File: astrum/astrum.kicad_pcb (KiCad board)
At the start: 2 copper layers, 32 parts, among them J1 USB_C_Receptacle_USB2.0_16P, J2 Micro_SD_Card, U1 STM32H523CEUx, U10 BSS138DW-7-F, U2 LDL212PV33R, U3 USBLC6-2SC6, U4 W25Q32JVSS, U5 ICM-20948, U6 MIC5317-1.8xM5, U7 BSS138DW-7-F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

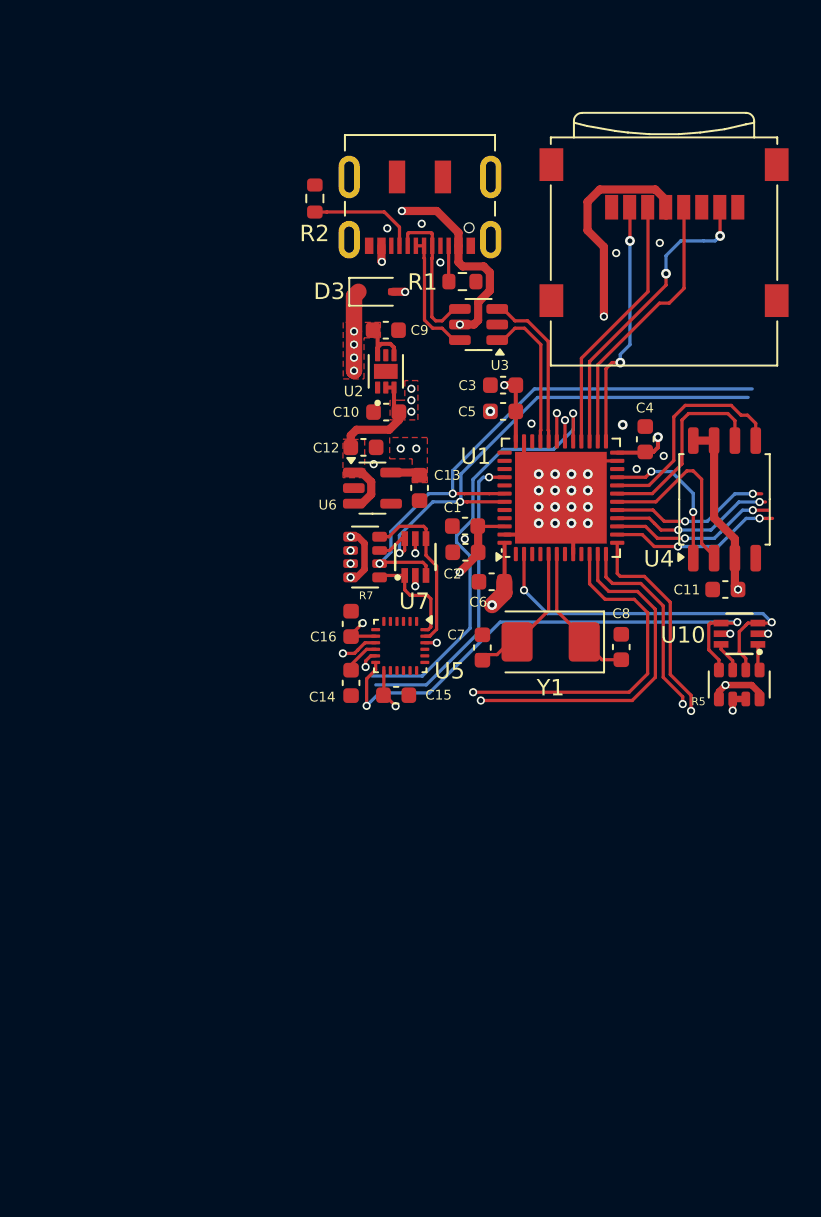
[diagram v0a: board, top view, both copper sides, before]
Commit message: add the drv routing and header pins + power supply
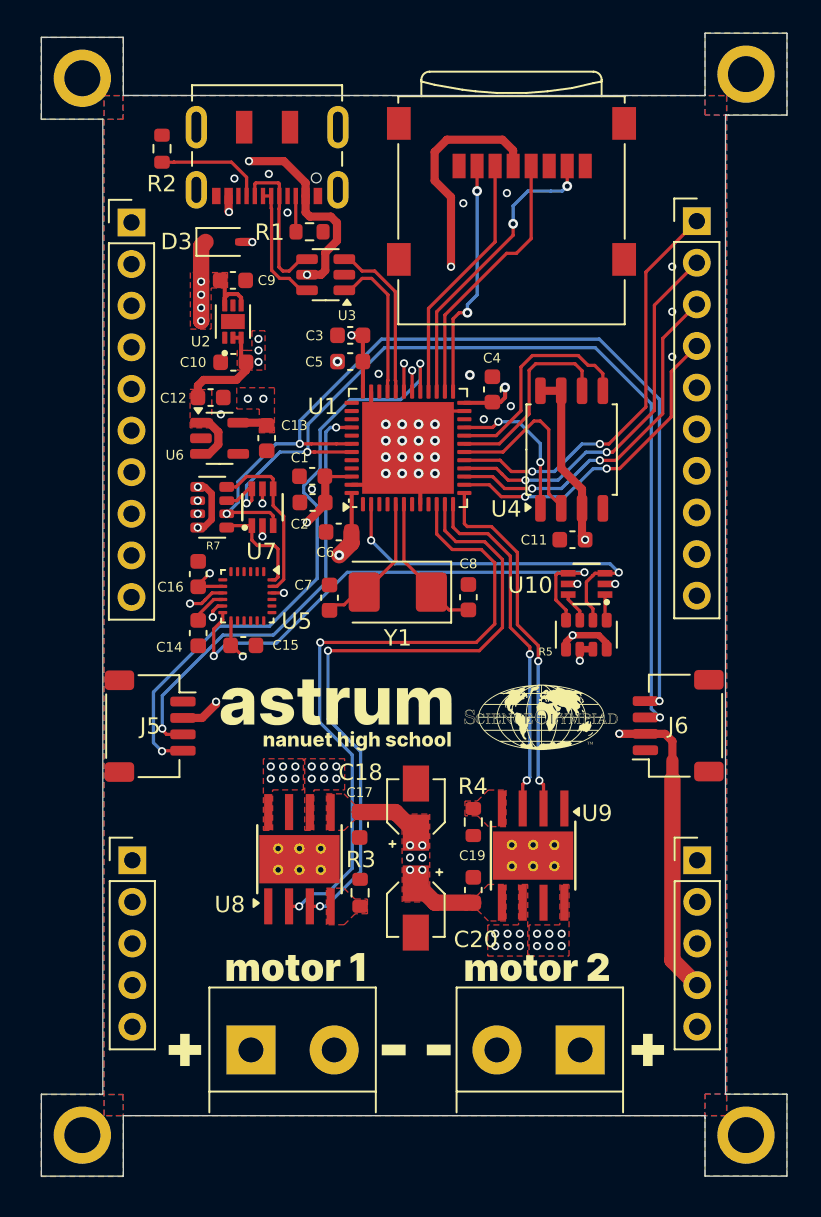
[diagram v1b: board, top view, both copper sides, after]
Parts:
- added C17: 100nF, A_HDJ_Library:C_0603_1608Metric, F.Cu at (142.4, 114.8)
- added C18: C_Polarized_Small, Capacitor_SMD:CP_Elec_3x5.3, F.Cu at (145.9, 113.8)
- added C19: 100nF, A_HDJ_Library:C_0603_1608Metric, F.Cu at (149.4, 118.8)
- added C20: C_Polarized_Small, Capacitor_SMD:CP_Elec_3x5.3, F.Cu at (145.8, 119.9)
- added G***: LOGO, LOGO, F.Cu at (153.5, 108.3)
- added G***: LOGO, LOGO, F.Cu at (144.5, 128.6)
- added G***: LOGO, LOGO, F.Cu at (153.2, 123.5)
- added G***: LOGO, LOGO, F.Cu at (143.2, 108.3)
- added G***: LOGO, LOGO, F.Cu at (131.8, 128.6)
- added G***: LOGO, LOGO, F.Cu at (160.0, 128.6)
- added G***: LOGO, LOGO, F.Cu at (147.2, 128.6)
- added G***: LOGO, LOGO, F.Cu at (138.5, 123.5)
- added H1: MountingHole_Pad_MP, MountingHole:MountingHole_2.2mm_M2_ISO7380_Pad, F.Cu at (125.5, 69.3)
- added H2: MountingHole_Pad_MP, MountingHole:MountingHole_2.2mm_M2_ISO7380_Pad, F.Cu at (166.0, 69.0)
- added H3: MountingHole_Pad_MP, MountingHole:MountingHole_2.2mm_M2_ISO7380_Pad, F.Cu at (166.0, 133.8)
- added H4: MountingHole_Pad_MP, MountingHole:MountingHole_2.2mm_M2_ISO7380_Pad, F.Cu at (125.5, 133.8)
- added J10: Conn_01x05_Pin, Connector_PinHeader_2.54mm:PinHeader_1x05_P2.54mm_Vertical, F.Cu at (163.0, 117.0)
- added J11: Screw_Terminal_01x02, TerminalBlock:TerminalBlock_bornier-2_P5.08mm, F.Cu at (155.9, 128.6)
- added J3: Screw_Terminal_01x02, TerminalBlock:TerminalBlock_bornier-2_P5.08mm, F.Cu at (135.8, 128.6)
- added J5: Conn_01x04_MountingPin, Connector_JST:JST_SH_SM04B-SRSS-TB_1x04-1MP_P1.00mm_Horizontal, F.Cu at (129.6, 108.8)
- added J6: Conn_01x04_MountingPin, Connector_JST:JST_SH_SM04B-SRSS-TB_1x04-1MP_P1.00mm_Horizontal, F.Cu at (161.9, 108.8)
- added J7: Conn_01x10_Pin, Connector_PinHeader_2.54mm:PinHeader_1x10_P2.54mm_Vertical, F.Cu at (163.0, 78.0)
- added J8: Conn_01x10_Pin, Connector_PinHeader_2.54mm:PinHeader_1x10_P2.54mm_Vertical, F.Cu at (128.5, 78.1)
- added J9: Conn_01x05_Pin, Connector_PinHeader_2.54mm:PinHeader_1x05_P2.54mm_Vertical, F.Cu at (128.6, 117.0)
- added R3: 30k, Resistor_SMD:R_0603_1608Metric, F.Cu at (142.4, 119.0)
- added R4: 30k, Resistor_SMD:R_0603_1608Metric, F.Cu at (149.4, 114.6)
- added U8: DRV8871DDA, Package_SO:Texas_HTSOP-8-1EP_3.9x4.9mm_P1.27mm_EP2.95x4.9mm_Mask2.4x3.1mm_ThermalVias, F.Cu at (138.7, 116.9)
- added U9: DRV8871DDA, Package_SO:Texas_HTSOP-8-1EP_3.9x4.9mm_P1.27mm_EP2.95x4.9mm_Mask2.4x3.1mm_ThermalVias, F.Cu at (153.0, 116.7)
- moved C12 9.81 mm to (133.3, 88.7)
- moved C11 9.81 mm to (155.4, 97.4)
- moved C14 9.81 mm to (132.6, 103.1)
- moved C16 9.81 mm to (132.6, 99.5)
- moved C3 9.81 mm to (141.8, 84.9)
- moved C5 9.81 mm to (141.8, 86.5)
- moved C9 9.81 mm to (134.7, 81.6)
- moved D3 9.81 mm to (134.1, 79.2)
- moved R5 9.81 mm to (156.3, 103.2)
- moved U2 9.81 mm to (134.7, 84.1)
- moved U3 9.81 mm to (140.3, 81.2)
- moved U4 9.81 mm to (155.4, 91.9)
- moved C15 9.81 mm to (135.3, 103.9)
- moved C2 9.81 mm to (139.6, 95.1)
- moved C8 9.81 mm to (149.1, 100.9)
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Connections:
- J2 pad 1: (no net) -> unconnected-(J2-DAT2-Pad1)
- J2 pad 2: (no net) -> Net-(J2-DAT3/CD)
- J2 pad 3: (no net) -> Net-(J2-CMD)
- J2 pad 4: (no net) -> VDD
- J2 pad 5: (no net) -> Net-(J2-CLK)
- J2 pad 6: (no net) -> GND
- J2 pad 7: (no net) -> Net-(J2-DAT0)
- J2 pad 8: (no net) -> unconnected-(J2-DAT1-Pad8)
- J2 pad 9: (no net) -> GND
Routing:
- net VDD: track 52.8 -> 175.6 mm, vias 12 -> 14
- net +BATT: track 8.70 -> 107.8 mm, vias 4 -> 10
- net +1V8: track 17.6 -> 93.4 mm
- net IMU_SDA: track 32.5 -> 58.3 mm, vias 2 -> 3
- net IMU_SCL: track 35.4 -> 61.1 mm, vias 2 -> 3
- net MOTOR1_PWM1: track 21.0 -> 40.4 mm, vias 1 -> 2
- net MOTOR1_PWM2: track 21.2 -> 39.5 mm, vias 1 -> 2
- net Net-(J3-Pin_2): track 0.00 -> 18.1 mm, vias 0 -> 6
- net Net-(J3-Pin_1): track 0.00 -> 17.4 mm, vias 0 -> 6
- net SPI1_MOSI: track 9.80 -> 25.6 mm
- net SPI1_MISO: track 10.1 -> 23.7 mm
- net SPI1_SCK: track 10.3 -> 21.8 mm
- net I2C3_SCL: track 27.1 -> 37.9 mm, vias 1 -> 2
- net MOTOR2_PWM1: track 12.1 -> 21.7 mm, vias 1 -> 2
- net SPI1_NSS: track 10.5 -> 19.9 mm
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- added copper zone on F.Cu, net +5V
- added copper zone on B.Cu, net GND
- added copper zone on F.Cu, net GND
- added copper zone on In1.Cu, net GND
- added copper zone on In2.Cu, net GND
- added copper zone on F.Cu, net Net-(J11-Pin_1)
- added copper zone on In2.Cu, net Net-(J11-Pin_1)
- added copper zone on F.Cu, net Net-(J11-Pin_2)
- added copper zone on In2.Cu, net Net-(J11-Pin_2)
- added copper zone on F.Cu, net Net-(J3-Pin_1)
- added copper zone on In2.Cu, net Net-(J3-Pin_1)
- added copper zone on F.Cu, net Net-(J3-Pin_2)
- added copper zone on In2.Cu, net Net-(J3-Pin_2)
- added copper zone on F.Cu, net Net-(U8-ILIM)
- added copper zone on F.Cu, net Net-(U9-ILIM)
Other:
- board outline added: 45.5 x 69.8 mm
- copper layers 2 -> 4
- board text added: "R3"

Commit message: add more gpio header things
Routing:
- net VDD: track 175.6 -> 177.7 mm
- net GND: vias 31 -> 30

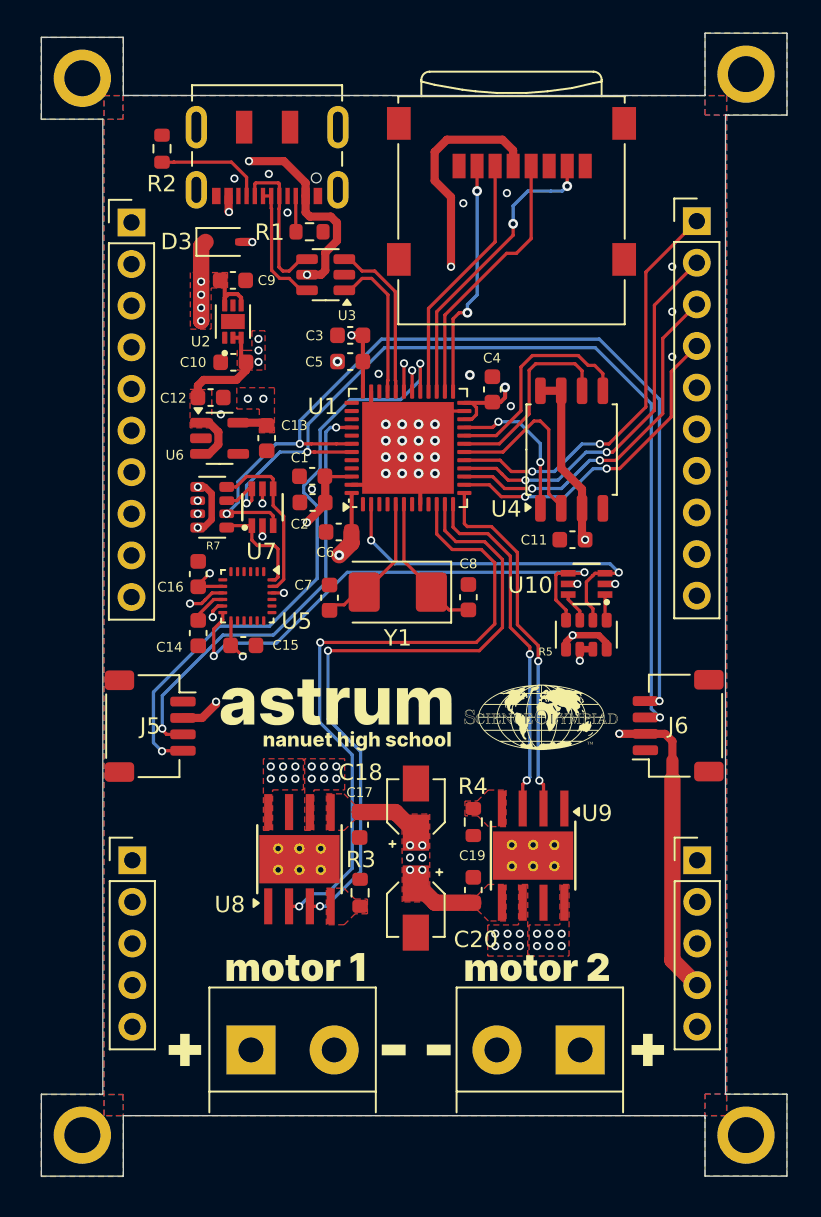
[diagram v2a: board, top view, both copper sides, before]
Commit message: fix the power plane and the mounting holes
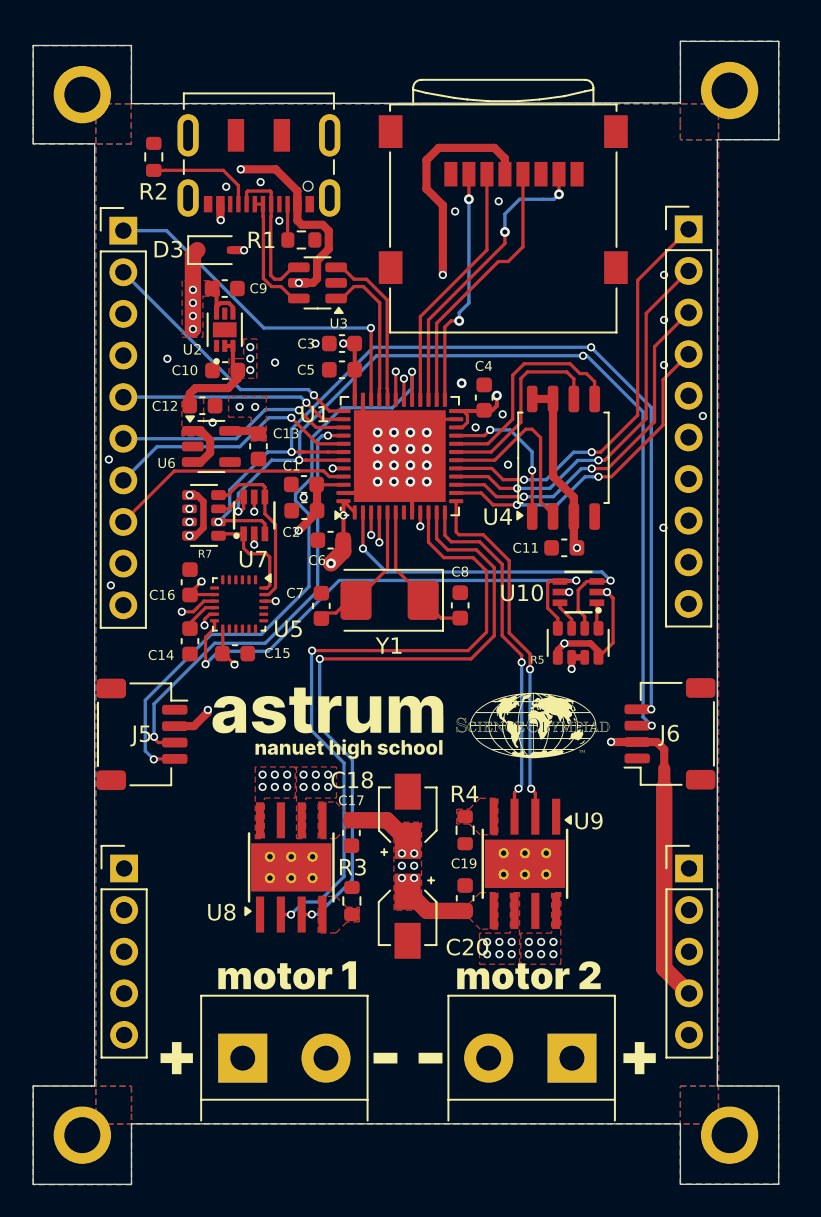
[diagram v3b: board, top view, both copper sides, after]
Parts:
- removed the G*** at (153.5, 108.3)
- removed the G*** at (144.5, 128.6)
- removed the G*** at (153.2, 123.5)
- removed the G*** at (143.2, 108.3)
- removed the G*** at (131.8, 128.6)
- removed the G*** at (160.0, 128.6)
- removed the G*** at (147.2, 128.6)
- removed the G*** at (138.5, 123.5)
- added G***: LOGO, LOGO, F.Cu at (152.8, 124.0)
- added G***: LOGO, LOGO, F.Cu at (146.8, 129.1)
- added G***: LOGO, LOGO, F.Cu at (144.0, 129.1)
- added G***: LOGO, LOGO, F.Cu at (153.0, 108.8)
- added G***: LOGO, LOGO, F.Cu at (159.5, 129.1)
- added G***: LOGO, LOGO, F.Cu at (142.8, 108.8)
- added G***: LOGO, LOGO, F.Cu at (138.0, 124.0)
- added G***: LOGO, LOGO, F.Cu at (131.2, 129.1)
- moved H2 1.41 mm to (165.0, 70.0)
- moved H1 1.00 mm to (125.5, 70.3)
- moved H3 1.00 mm to (165.0, 133.8)
- moved C1 0.71 mm to (139.0, 94.0)
- moved C10 0.71 mm to (134.2, 87.1)
- moved C11 0.71 mm to (154.9, 97.9)
- moved C12 0.71 mm to (132.8, 89.2)
- moved C13 0.71 mm to (136.2, 91.7)
- moved C14 0.71 mm to (132.1, 103.6)
- moved C15 0.71 mm to (134.8, 104.4)
- moved C16 0.71 mm to (132.1, 100.0)
- moved C17 0.71 mm to (141.9, 115.3)
- moved C18 0.71 mm to (145.4, 114.3)
- moved C19 0.71 mm to (148.9, 119.3)
- moved C2 0.71 mm to (139.1, 95.6)
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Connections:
- J7 pad 5: unconnected-(J7-Pin_5-Pad5) -> IMU_SCL
- J7 pad 6: unconnected-(J7-Pin_6-Pad6) -> IMU_SDA
- J7 pad 7: unconnected-(J7-Pin_7-Pad7) -> I2C3_SCL
- J7 pad 8: unconnected-(J7-Pin_8-Pad8) -> I2C3_SDA
- J8 pad 1: unconnected-(J8-Pin_1-Pad1) -> SWDIO
- J8 pad 10: unconnected-(J8-Pin_10-Pad10) -> GPIO8
- J8 pad 2: unconnected-(J8-Pin_2-Pad2) -> SWCLK
- J8 pad 3: unconnected-(J8-Pin_3-Pad3) -> GPIO1
- J8 pad 4: unconnected-(J8-Pin_4-Pad4) -> GPIO2
- J8 pad 5: unconnected-(J8-Pin_5-Pad5) -> GPIO3
- J8 pad 6: unconnected-(J8-Pin_6-Pad6) -> GPIO4
- J8 pad 7: unconnected-(J8-Pin_7-Pad7) -> GPIO5
- J8 pad 8: unconnected-(J8-Pin_8-Pad8) -> GPIO6
- J8 pad 9: unconnected-(J8-Pin_9-Pad9) -> GPIO7
- U1 pad 3: unconnected-(U1-PC14-Pad3) -> GPIO7
- U1 pad 30: unconnected-(U1-PA9-Pad30) -> GPIO2
- U1 pad 31: unconnected-(U1-PA10-Pad31) -> GPIO1
- U1 pad 34: unconnected-(U1-PA13(JTMS-Pad34) -> SWDIO
- U1 pad 37: unconnected-(U1-PA14(JTCK-Pad37) -> SWCLK
- U1 pad 38: unconnected-(U1-PA15(JTDI)-Pad38) -> GPIO3
- U1 pad 39: unconnected-(U1-PB3(JTDO-Pad39) -> GPIO4
- U1 pad 4: unconnected-(U1-PC15-Pad4) -> GPIO8
- U1 pad 41: unconnected-(U1-PB5-Pad41) -> GPIO5
- U1 pad 45: unconnected-(U1-PB8-Pad45) -> GPIO6
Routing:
- net VDD: track 177.7 -> 89.9 mm, vias 14 -> 16
- net I2C3_SCL: track 37.9 -> 83.1 mm
- net I2C3_SDA: track 27.2 -> 68.1 mm
- net SWDIO: track 0.00 -> 22.0 mm, vias 0 -> 1
- net GPIO1: track 0.00 -> 19.8 mm, vias 0 -> 1
- net GPIO8: track 0.00 -> 19.7 mm, vias 0 -> 1
- net GPIO2: track 0.00 -> 19.1 mm, vias 0 -> 1
- net GPIO7: track 0.00 -> 17.2 mm, vias 0 -> 1
- net SWCLK: track 0.00 -> 17.0 mm, vias 0 -> 1
- net GPIO5: track 0.00 -> 15.7 mm, vias 0 -> 1
- net GPIO6: track 0.00 -> 14.9 mm
- net GPIO4: track 0.00 -> 14.6 mm, vias 0 -> 1
- net GPIO3: track 0.00 -> 14.0 mm, vias 0 -> 1
- net IMU_SDA: track 58.3 -> 66.8 mm, vias 3 -> 4
- net IMU_SCL: track 61.1 -> 68.3 mm, vias 3 -> 4
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- added copper zone on In2.Cu, net VDD
- removed copper zone on F.Cu, net +5V
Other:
- outline, holes or cut-outs redrawn
